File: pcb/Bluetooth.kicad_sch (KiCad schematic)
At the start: 18 parts, among them U12 74HC2G14, U13 74HC2G14, U14 RN4678

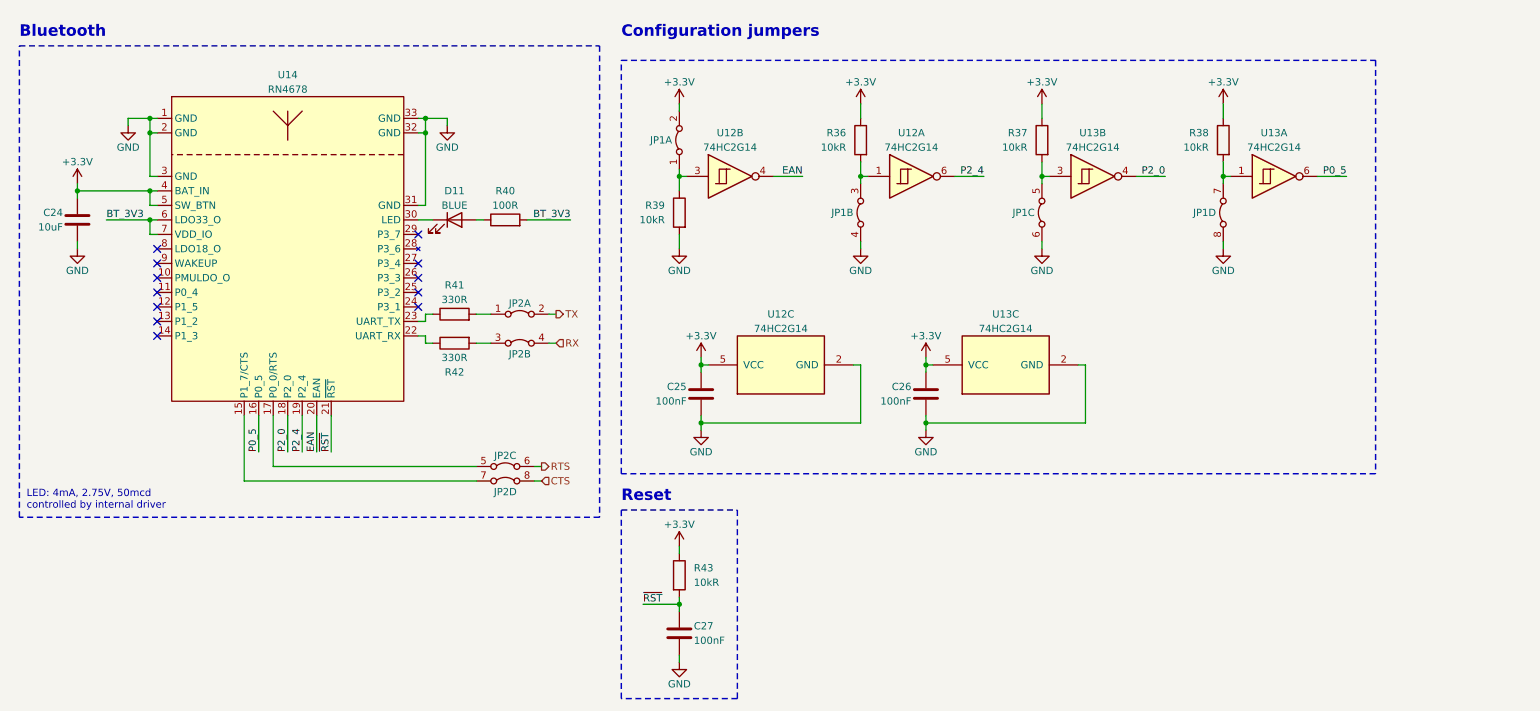
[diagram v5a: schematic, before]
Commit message: [pcb] More final touches, UART test ponts added.
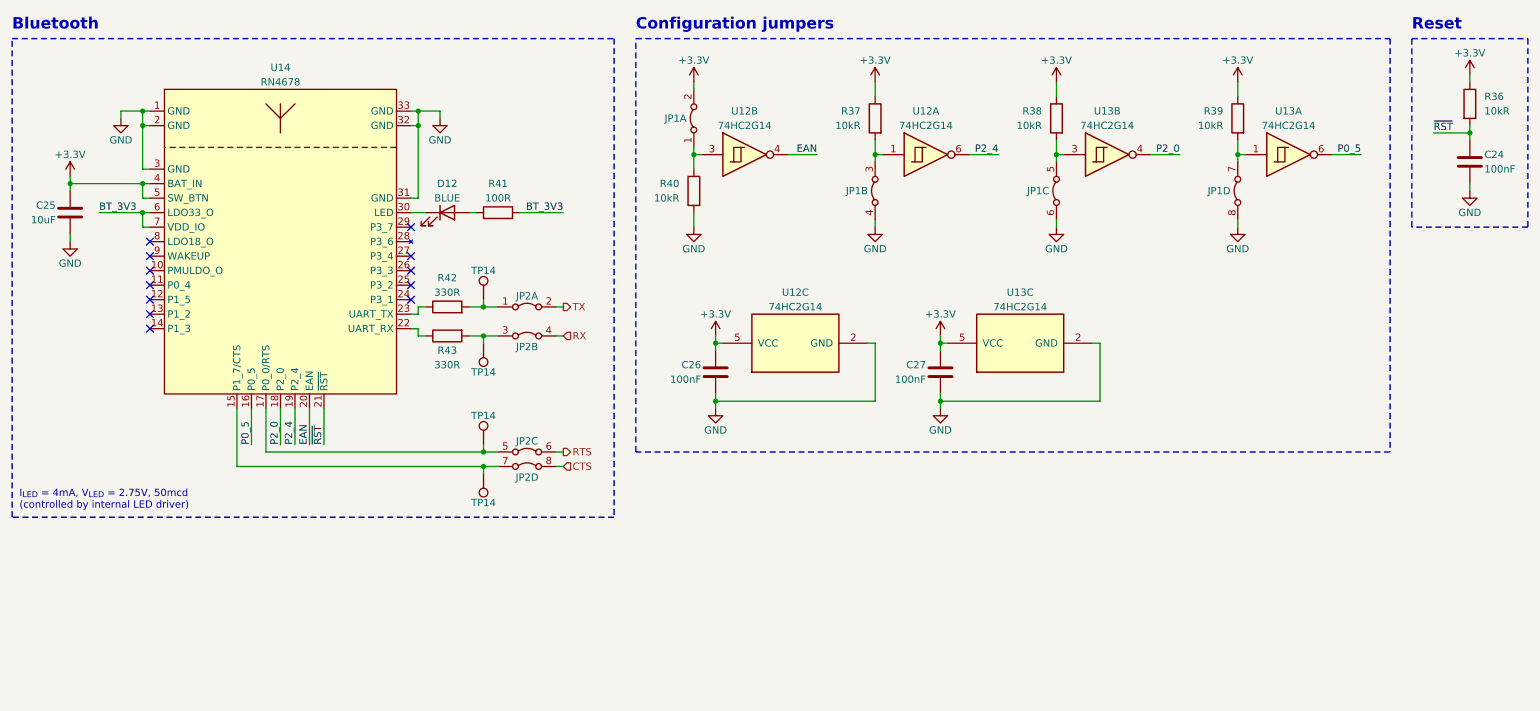
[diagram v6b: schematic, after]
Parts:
- added TP14 (x4): TestPoint, TestPoint:TestPoint_Pad_D2.0mm, symbol Connector:TestPoint
- renumbered C27 to C24, C24 to C25, C25 to C26, C26 to C27, D11 to D12, R43 to R36, R36 to R37, R37 to R38, R38 to R39, R39 to R40, R40 to R41, R41 to R42, R42 to R43
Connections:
- net at JP2.3, R43.2: now also TP14.1
- net at JP2.7, U14.15 (P1_7/CTS): now also TP14.1
- net at JP2.5, U14.17 (P0_0/RTS): now also TP14.1
- net at JP2.1, R42.2: now also TP14.1
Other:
- note added: "I_{LED} = 4mA, V_{LED} = 2.75V, 50mcd (controlled by internal LED driver)"
- note removed: "LED: 4mA, 2.75V, 50mcd controlled by internal driver"
- moved on the sheet: C24, C25, C26, C27, D12, JP1A, JP1B, JP1C, JP1D, JP2A, JP2B, JP2C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

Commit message: [pcb] 10uF capacitor changed from A to T package
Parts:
- C25: footprint Capacitor_Tantalum_SMD:CP_EIA-3216-18_Kemet-A -> Capacitor_Tantalum_SMD:CP_EIA-3528-12_Kemet-T
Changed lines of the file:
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@@
       (effects (font (size 1.27 1.27)) (justify left))
     )
-    (property "Footprint" "Capacitor_Tantalum_SMD:CP_EIA-3216-18_Kemet-A" (at 25.7048 54.61 0)
+    (property "Footprint" "Capacitor_Tantalum_SMD:CP_EIA-3528-12_Kemet-T" (at 25.7048 54.61 0)
       (effects (font (size 1.27 1.27)) hide)
     )
